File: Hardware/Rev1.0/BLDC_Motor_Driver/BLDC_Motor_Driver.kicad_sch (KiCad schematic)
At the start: 54 parts, among them Q1 NMOS, Q2 NMOS, Q3 NMOS, Q4 NMOS, Q5 NMOS, Q6 NMOS, U1 STM32F446RETx, U2 SPB09B-03

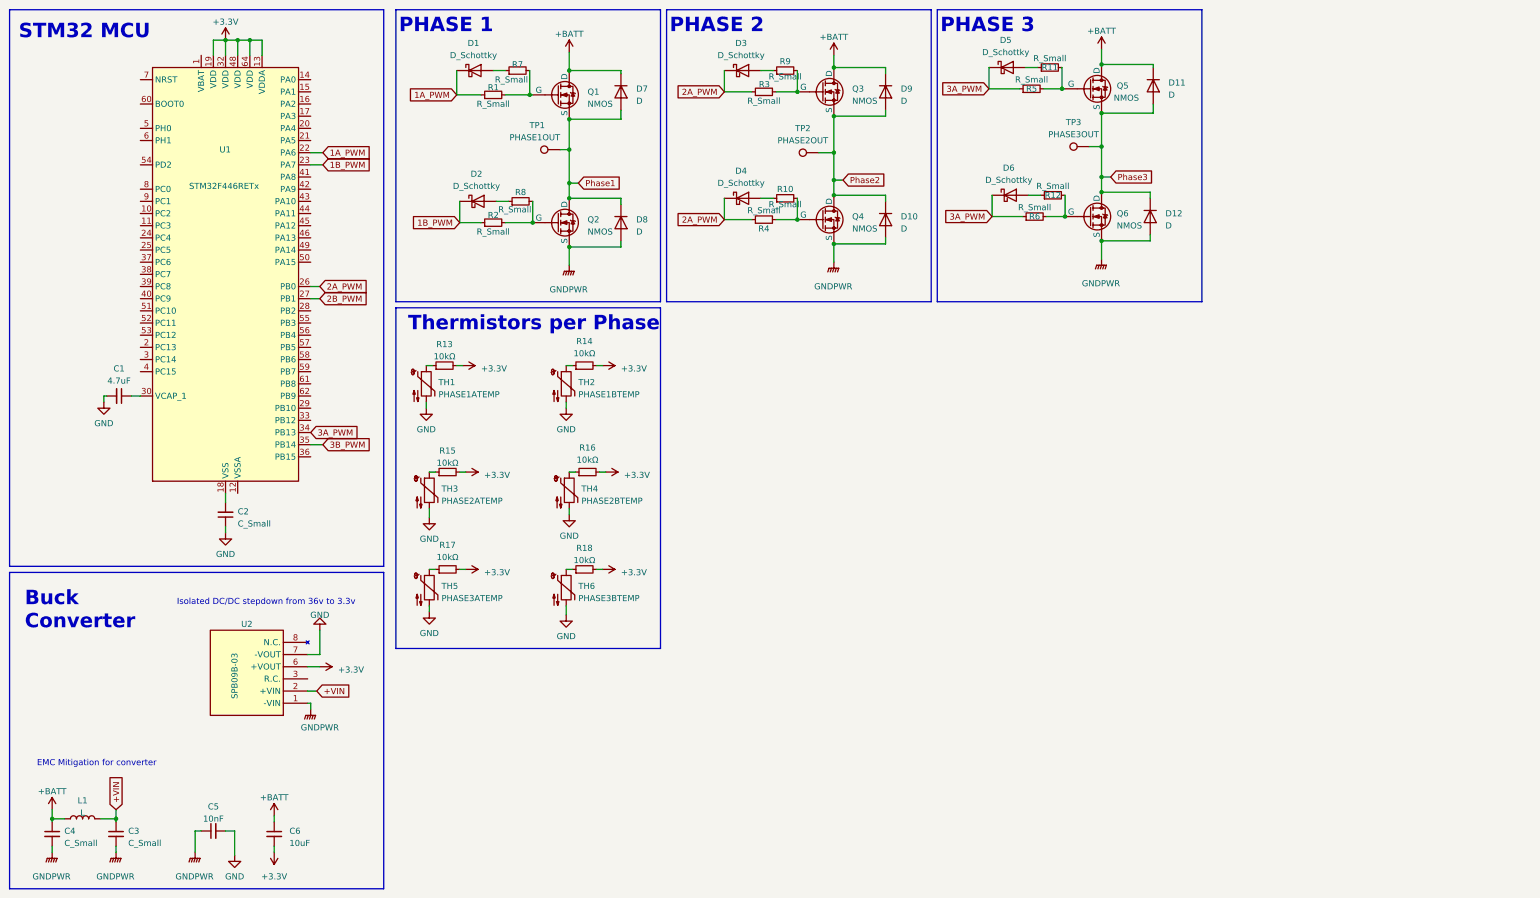
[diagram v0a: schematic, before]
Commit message: Updates to Stages and MCU inputs
Selected NMOS's and added basis for back EMF
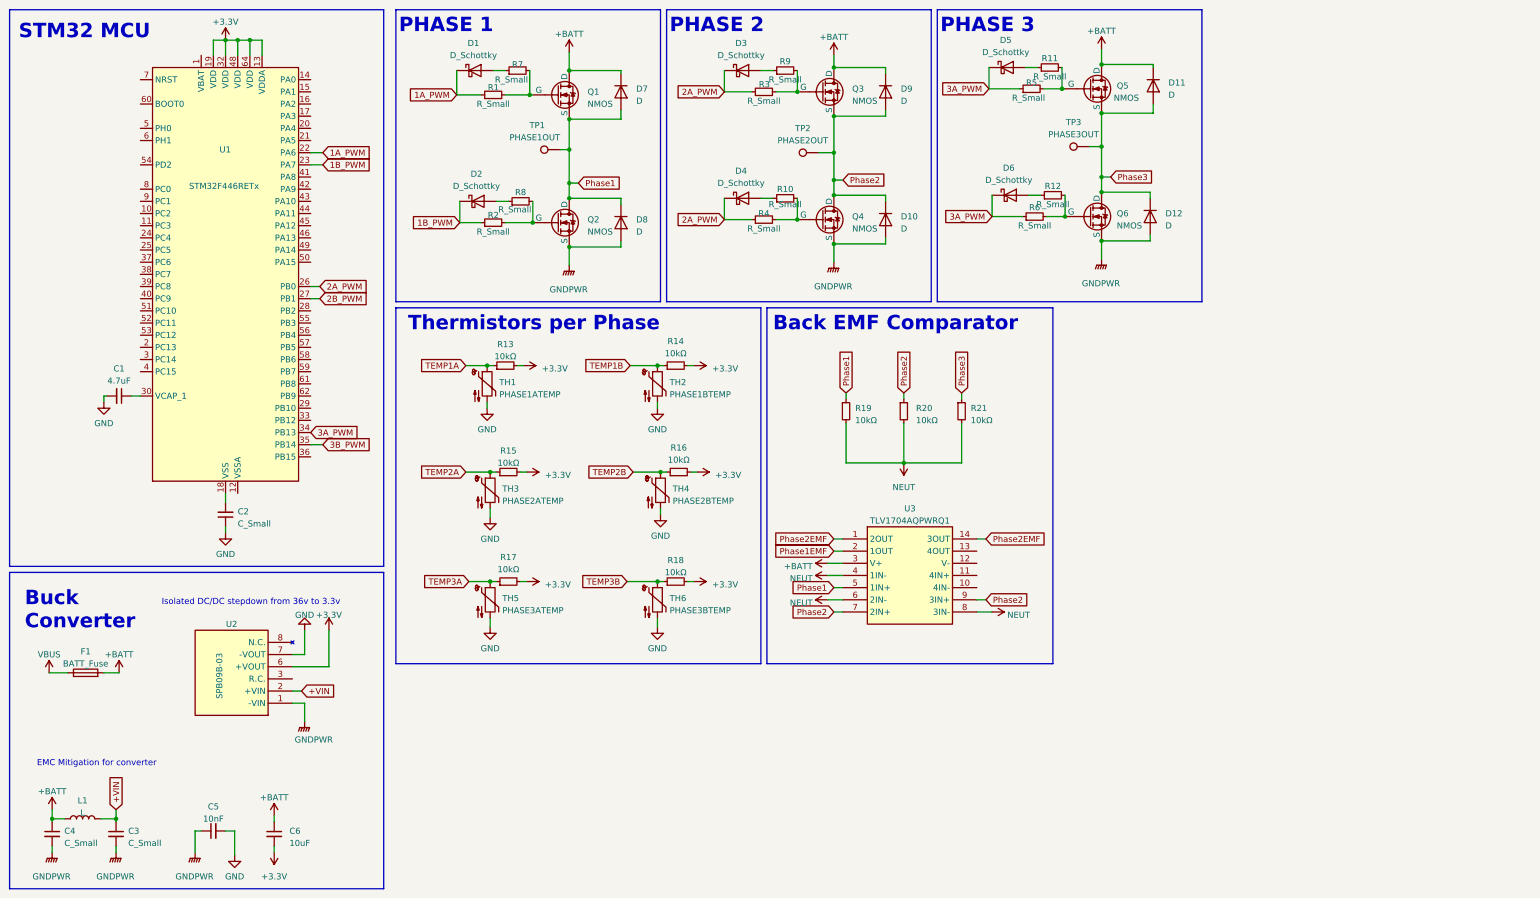
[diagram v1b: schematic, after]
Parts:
- added F1: BATT_Fuse, Fuse:3557-2, symbol Device:Fuse
- added R19, R20, R21: 10kΩ, Resistor_SMD:R_0603_1608Metric, symbol Device:R_Small
- added U3: TLV1704AQPWRQ1, Package_SO:SOP65P640X120-14N, symbol Comparator:TLV1704AQPWRQ1
- Q1, Q2, Q3, Q4, Q5, Q6: footprint (none) -> Package_TO_SOT_SMD:IPD90N06S4L03
- R1, R10, R11, R12, R13, R14, R15, R16, R17, R18, R2, R3, R4, R5, R6, R7, R8, R9: footprint (none) -> Resistor_SMD:R_0603_1608Metric
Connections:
- net +BATT: now also F1.2, U3.3 (V+)
- net Phase1: now also R19.1, U3.5 (1IN+)
- net Phase2: now also R20.1, U3.7 (2IN+), U3.9 (3IN+)
- net Phase3: now also R21.1
- net TEMP3A: now reaches R17.1, TH5.1
- net TEMP1A: now reaches R13.1, TH1.1
- net TEMP3B: now reaches R18.1, TH6.1
- net TEMP2B: now reaches R16.1, TH4.1
- net TEMP1B: now reaches R14.1, TH2.1
- net TEMP2A: now reaches R15.1, TH3.1
- new net NEUT: R19.2, R20.2, R21.2, U3.4 (1IN-), U3.6 (2IN-), U3.8 (3IN-)
- new net Phase1EMF: U3.2 (1OUT)
- new net Phase2EMF: U3.1 (2OUT), U3.14 (3OUT)
- new net VBUS: F1.1
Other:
- note added: "Back EMF Comparator"
- moved on the sheet: R13, R14, R15, R16, R17, R18, TH1, TH2, TH3, TH4, TH5, TH6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

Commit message: Added changes to schematic (20% competed)
Updated datasheets and schematic symbols for the NMOS FETs. Still need to establish resistor values.
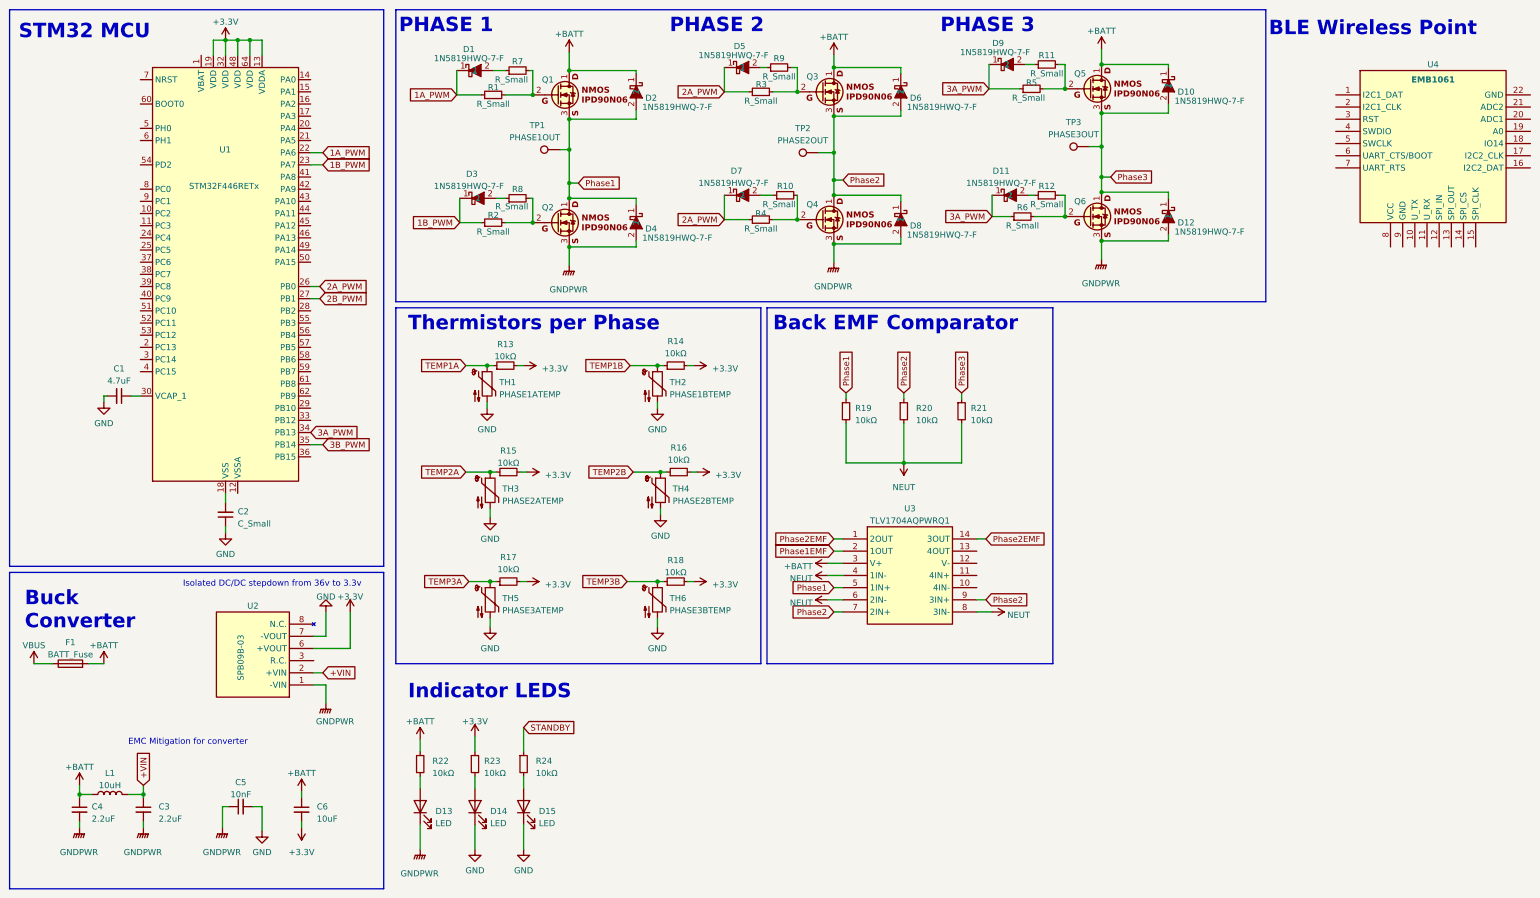
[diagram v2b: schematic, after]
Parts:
- removed D1, D2, D3, D4, D5, D6: D_Schottky, symbol Device:D_Schottky
- removed D10, D11, D12, D7, D8, D9: D, symbol Device:D
- removed Q1, Q2, Q3, Q4, Q5, Q6: NMOS, Package_TO_SOT_SMD:IPD90N06S4L03, symbol Simulation_SPICE:NMOS
- added D1, D10, D11, D12, D2, D3, D4, D5, D6, D7, D8, D9: 1N5819HWQ-7-F, Diode_SMD:SOD3716X145N, symbol Diode:1N5819HWQ-7-F
- added D13, D14, D15: LED, LED_SMD:LED_0603_1608Metric, symbol Device:LED
- added Q1, Q2, Q3, Q4, Q5, Q6: IPD90N06S4L03ATMA2, Package_TO_SOT_SMD:IPD90N06S4L03, symbol Transistor_FET:IPD90N06S4L03ATMA2
- added R22, R23, R24: 10kΩ, Resistor_SMD:R_0603_1608Metric, symbol Device:R_Small
- added U4: EMB1061, RF_Module:EMB1061, symbol RF_Bluetooth:EMB1061
- C1, C2, C5: footprint (none) -> Capacitor_SMD:C_0603_1608Metric
- C3, C4: value C_Small -> 2.2uF; footprint (none) -> Capacitor_SMD:C_0603_1608Metric
- L1: value L -> 10uH; footprint (none) -> Inductor_SMD:SRP06152R2K
- TH1, TH2, TH3, TH4, TH5, TH6: footprint (none) -> Resistor_SMD:R_0603_1608Metric
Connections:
- net +3.3V: now also R23.1
- net +BATT: now also D10.1, D2.1, D6.1, Q1.1, Q3.1, Q5.1, R22.1
- net 1A_PWM: now also D1.1
- net 1B_PWM: now also D3.1
- net 2A_PWM: now also D5.1, D7.1
- net 3A_PWM: now also D11.1, D9.1
- net GND: now also D14.1 (K), D15.1 (K)
- net GNDPWR: now also D12.2, D13.1 (K), D4.2, D8.2, Q2.3, Q4.3, Q6.3
- net Phase1: now also D2.2, D4.1, Q1.3, Q2.1
- net Phase2: now also D6.2, D8.1, Q3.3, Q4.1
- net Phase3: now also D10.2, D12.1, Q5.3, Q6.1
- net at R9.1: now also D5.2
- net at R12.1: now also D11.2
- net at R7.1: now also D1.2
- net at R1.2, R7.2: now also Q1.2
- net at R3.2, R9.2: now also Q3.2
- net at R12.2, R6.2: now also Q6.2
- net at R10.2, R4.2: now also Q4.2
- net at R11.2, R5.2: now also Q5.2
- net at R2.2, R8.2: now also Q2.2
- net at R10.1: now also D7.2
- net at R11.1: now also D9.2
- net at R8.1: now also D3.2
- new net: D14.2 (A), R23.2
- new net: D13.2 (A), R22.2
- new net: D15.2 (A), R24.2
- new net STANDBY: R24.1
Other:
- note added: "BLE Wireless Point"
- note added: "Indicator LEDS"
- moved on the sheet: C3, C4, C5, C6, F1, L1, R10, R11, R12, R3, R4, R6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

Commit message: Schematic Updates (MOSFETs)
Assigned preliminary rlimit values, modified some footprint placements, and fixed a MOSFET misassignment for schematics.
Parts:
- removed U4: EMB1061, RF_Module:EMB1061, symbol RF_Bluetooth:EMB1061
- C6: footprint (none) -> Capacitor_SMD:C_0603_1608Metric
- R1, R10, R11, R12, R2, R3, R4, R5, R6, R7, R8, R9: value R_Small -> 100Ω
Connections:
- net +BATT: now also Q1.2, Q3.2, Q5.2; no longer Q1.1, Q3.1, Q5.1
- net Phase1: now also Q2.2; no longer Q2.1
- net Phase2: now also Q4.2; no longer Q4.1
- net Phase3: now also Q6.2; no longer Q6.1
- net at R2.2, R8.2: now also Q2.1; no longer Q2.2
- net at R3.2, R9.2: now also Q3.1; no longer Q3.2
- net at R1.2, R7.2: now also Q1.1; no longer Q1.2
- net at R12.2, R6.2: now also Q6.1; no longer Q6.2
- net at R10.2, R4.2: now also Q4.1; no longer Q4.2
- net at R11.2, R5.2: now also Q5.1; no longer Q5.2

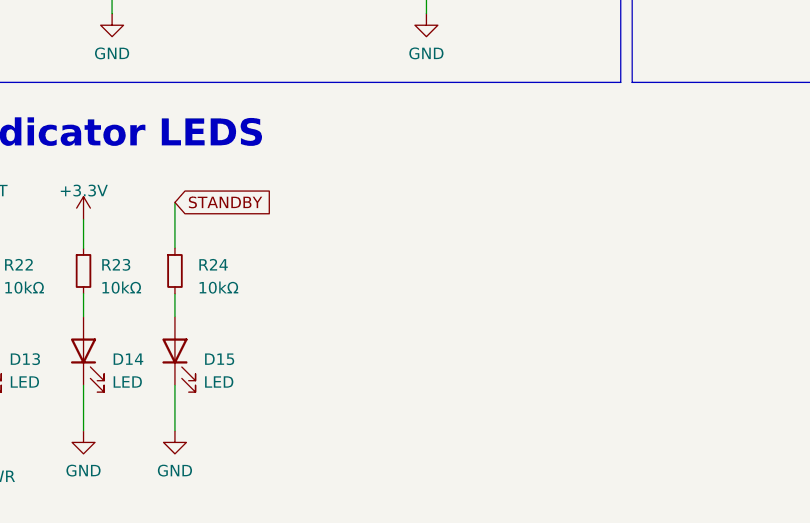
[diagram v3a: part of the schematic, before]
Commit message: Started some PCB edits
Minor PCB layout edits
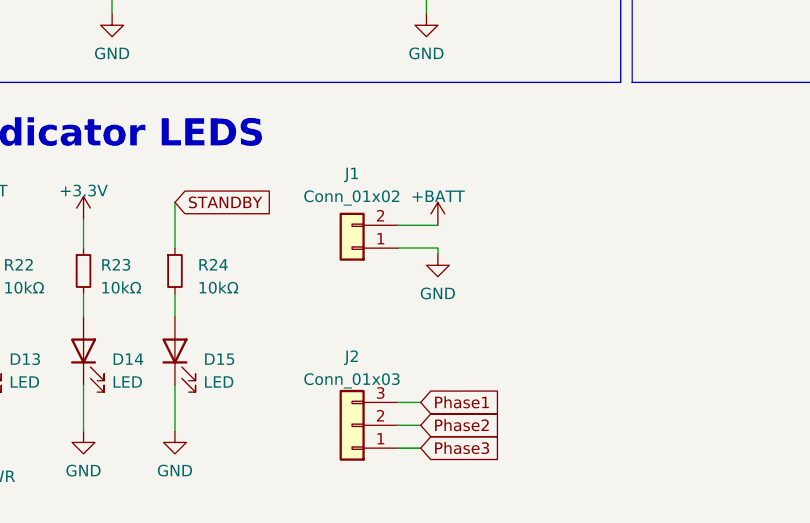
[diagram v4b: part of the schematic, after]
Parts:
- added J1: Conn_01x02, symbol Connector_Generic:Conn_01x02
- added J2: Conn_01x03, symbol Connector_Generic:Conn_01x03
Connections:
- net +BATT: now also J1.2 (Pin_2)
- net GND: now also J1.1 (Pin_1)
- net Phase1: now also J2.3 (Pin_3)
- net Phase2: now also J2.2 (Pin_2)
- net Phase3: now also J2.1 (Pin_1)
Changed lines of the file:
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@@
+    (stroke (width 0) (type default))
+  )
+  (wire (pts (xy 147.955 185.42) (xy 145.415 185.42))
     (stroke (width 0) (type default))
   )
@@
     (stroke (width 0) (type default))
   )
+  (wire (pts (xy 149.86 168.91) (xy 149.86 168.275))
+    (stroke (width 0) (type default))
+  )
   (wire (pts (xy 144.145 53.975) (xy 144.145 52.705))
     (stroke (width 0) (type default))
@@
     (stroke (width 0) (type default))
   )
+  (wire (pts (xy 149.86 168.275) (xy 145.415 168.275))
+    (stroke (width 0) (type default))
+  )
   (wire (pts (xy 255.27 24.765) (xy 241.3 24.765))
     (stroke (width 0) (type default))
@@
     (stroke (width 0) (type default))
   )
+  (wire (pts (xy 147.955 187.96) (xy 145.415 187.96))
+    (stroke (width 0) (type default))
+  )
   (wire (pts (xy 27.94 182.88) (xy 27.94 184.15))
     (stroke (width 0) (type default))
@@
     (stroke (width 0) (type default))
   )
+  (wire (pts (xy 145.415 165.735) (xy 149.86 165.735))
+    (stroke (width 0) (type default))
+  )
   (wire (pts (xy 60.96 19.685) (xy 63.5 19.685))
     (stroke (width 0) (type default))
@@
   )
   (wire (pts (xy 212.09 107.95) (xy 200.025 107.95))
+    (stroke (width 0) (type default))
+  )
+  (wire (pts (xy 147.955 190.5) (xy 145.415 190.5))
     (stroke (width 0) (type default))
   )
@@
     (effects (font (size 1.27 1.27)) (justify left))
     (property "Intersheetrefs" "${INTERSHEET_REFS}" (at 86.5443 101.6 0)
+      (effects (font (size 1.27 1.27)) (justify left) hide)
+    )
+  )
+  (global_label "Phase2" (shape input) (at 147.955 187.96 0) (fields_autoplaced)
+    (effects (font (size 1.27 1.27)) (justify left))
+    (property "Intersheetrefs" "${INTERSHEET_REFS}" (at 157.755 187.96 0)
       (effects (font (size 1.27 1.27)) (justify left) hide)
     )
@@
     )
   )
+  (global_label "Phase3" (shape input) (at 147.955 190.5 0) (fields_autoplaced)
+    (effects (font (size 1.27 1.27)) (justify left))
+    (property "Intersheetrefs" "${INTERSHEET_REFS}" (at 157.755 190.5 0)
+      (effects (font (size 1.27 1.27)) (justify left) hide)
+    )
+  )
   (global_label "3A_PWM" (shape input) (at 218.44 56.515 180) (fields_autoplaced)
     (effects (font (size 1.27 1.27)) (justify right))
@@
     )
   )
+  (global_label "Phase1" (shape input) (at 147.955 185.42 0) (fields_autoplaced)
+    (effects (font (size 1.27 1.27)) (justify left))
+    (property "Intersheetrefs" "${INTERSHEET_REFS}" (at 157.755 185.42 0)
+      (effects (font (size 1.27 1.27)) (justify left) hide)
+    )
+  )
   (global_label "2A_PWM" (shape input) (at 162.56 30.48 180) (fields_autoplaced)
     (effects (font (size 1.27 1.27)) (justify right))
@@
         (path "/596d4d2f-9b45-4ea8-aaa3-44fe771f8415"
           (reference "#PWR05") (unit 1)
+        )
+      )
+    )
+  )
+  (symbol (lib_id "Connector_Generic:Conn_01x02") (at 140.335 168.275 180) (unit 1)
+    (in_bom yes) (on_board yes) (dnp no) (fields_autoplaced)
+    (property "Reference" "J1" (at 140.335 160.02 0)
+      (effects (font (size 1.27 1.27)))
+    )
+    (property "Value" "Conn_01x02" (at 140.335 162.56 0)
+      (effects (font (size 1.27 1.27)))
+    )
+    (property "Footprint" "" (at 140.335 168.275 0)
+      (effects (font (size 1.27 1.27)) hide)
+    )
+    (property "Datasheet" "~" (at 140.335 168.275 0)
+      (effects (font (size 1.27 1.27)) hide)
+    )
+    (pin "1")
+    (pin "2")
+    (instances
+      (project "BLDC_Motor_Driver"
+        (path "/596d4d2f-9b45-4ea8-aaa3-44fe771f8415"
+          (reference "J1") (unit 1)
         )
       )
@@
     )
   )
+  (symbol (lib_id "power:+BATT") (at 149.86 165.735 0) (unit 1)
+    (in_bom yes) (on_board yes) (dnp no)
+    (property "Reference" "#PWR044" (at 149.86 169.545 0)
+      (effects (font (size 1.27 1.27)) hide)
+    )
+    (property "Value" "+BATT" (at 149.86 162.56 0)
+      (effects (font (size 1.27 1.27)))
+    )
+    (property "Footprint" "" (at 149.86 165.735 0)
+      (effects (font (size 1.27 1.27)) hide)
+    )
+    (property "Datasheet" "" (at 149.86 165.735 0)
+      (effects (font (size 1.27 1.27)) hide)
+    )
+    (pin "1")
+    (instances
+      (project "BLDC_Motor_Driver"
+        (path "/596d4d2f-9b45-4ea8-aaa3-44fe771f8415"
+          (reference "#PWR044") (unit 1)
+        )
+      )
+    )
+  )
   (symbol (lib_id "Device:R_Small") (at 117.475 132.715 90) (unit 1)
     (in_bom yes) (on_board yes) (dnp no) (fields_autoplaced)
@@
     )
   )
+  (symbol (lib_id "Connector_Generic:Conn_01x03") (at 140.335 187.96 180) (unit 1)
+    (in_bom yes) (on_board yes) (dnp no) (fields_autoplaced)
+    (property "Reference" "J2" (at 140.335 180.34 0)
+      (effects (font (size 1.27 1.27)))
+    )
+    (property "Value" "Conn_01x03" (at 140.335 182.88 0)
+      (effects (font (size 1.27 1.27)))
+    )
+    (property "Footprint" "" (at 140.335 187.96 0)
+      (effects (font (size 1.27 1.27)) hide)
+    )
+    (property "Datasheet" "~" (at 140.335 187.96 0)
+      (effects (font (size 1.27 1.27)) hide)
+    )
+    (pin "1")
+    (pin "2")
+    (pin "3")
+    (instances
+      (project "BLDC_Motor_Driver"
+        (path "/596d4d2f-9b45-4ea8-aaa3-44fe771f8415"
+          (reference "J2") (unit 1)
+        )
+      )
+    )
+  )
   (symbol (lib_id "Transistor_FET:IPD90N06S4L03ATMA2") (at 241.3 29.845 0) (unit 1)
     (in_bom yes) (on_board yes) (dnp no)
@@
         )
       )
+    )
+  )
+  (symbol (lib_id "power:GND") (at 149.86 168.91 0) (unit 1)
+    (in_bom yes) (on_board yes) (dnp no) (fields_autoplaced)
+    (property "Reference" "#PWR046" (at 149.86 175.26 0)
+      (effects (font (size 1.27 1.27)) hide)
+    )
+    (property "Value" "GND" (at 149.86 173.355 0)
+      (effects (font (size 1.27 1.27)))
+    )
+    (property "Footprint" "" (at 149.86 168.91 0)
+      (effects (font (size 1.27 1.27)) hide)
+    )
+    (property "Datasheet" "" (at 149.86 168.91 0)
+      (effects (font (size 1.27 1.27)) hide)
+    )
+    (pin "1")
+    (instances
+      (project "BLDC_Motor_Driver"
+        (path "/596d4d2f-9b45-4ea8-aaa3-44fe771f8415"
+          (reference "#PWR046") (unit 1)
+        )
+      )
